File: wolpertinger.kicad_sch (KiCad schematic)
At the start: 19 parts, among them IC1 TL074

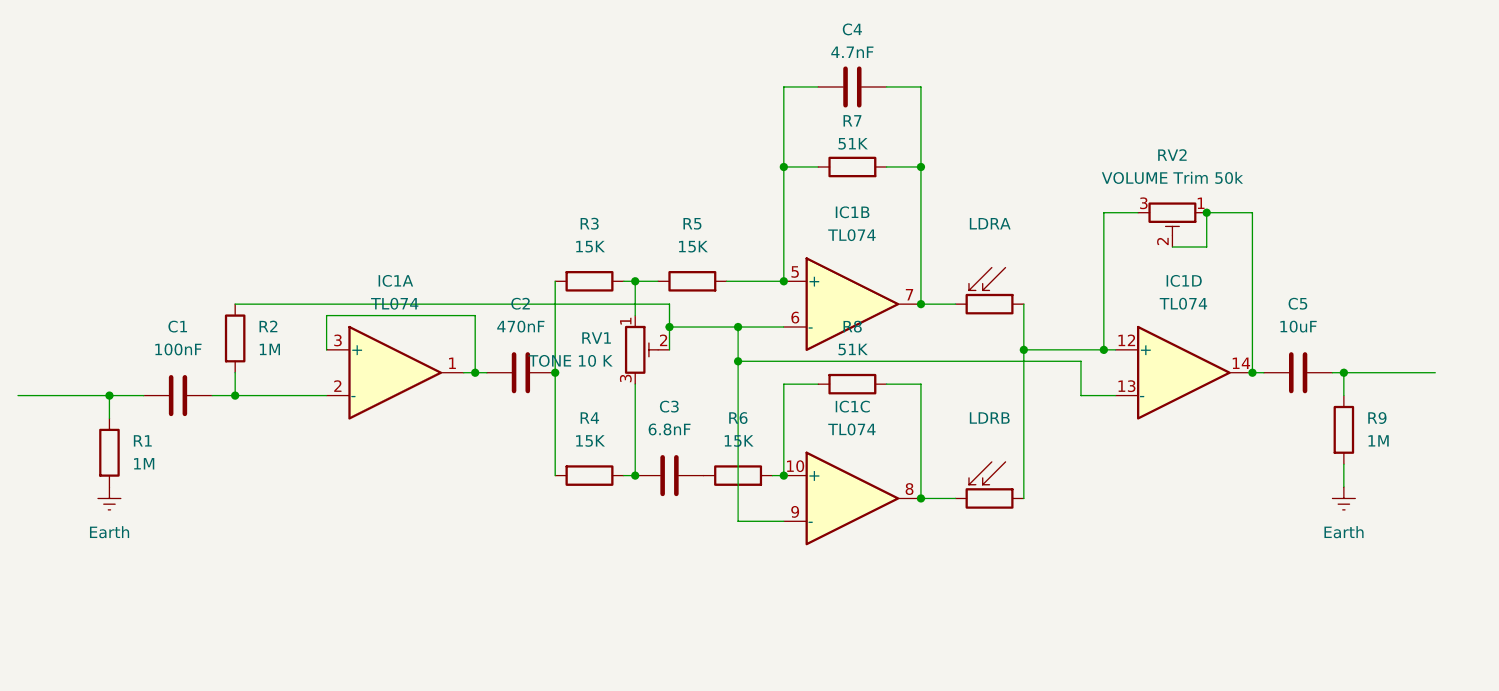
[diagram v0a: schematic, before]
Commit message: add gitignore and schematic cleanup
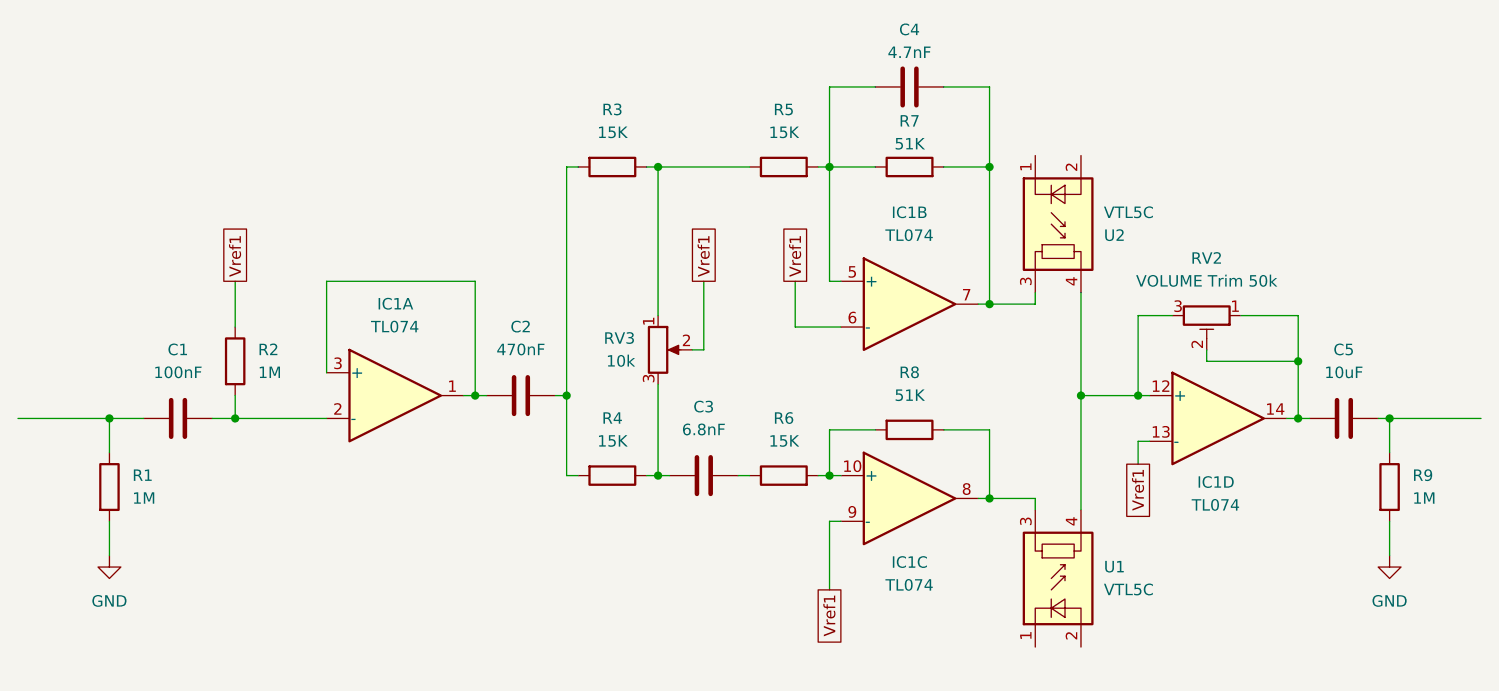
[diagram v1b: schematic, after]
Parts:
- removed LDRA, LDRB: (no value), OptoDevice:R_LDR_5.1x4.3mm_P3.4mm_Vertical, symbol Sensor_Optical:LDR07
- removed RV1: TONE 10 K, symbol Device:R_Potentiometer_Trim
- added RV3: 10k, symbol Device:R_Potentiometer
- added U1, U2: VTL5C, OptoDevice:PerkinElmer_VTL5C, symbol Isolator:VTL5C
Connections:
- net at R3.1, R5.1: now also RV3.1
- net Vref1: now reaches IC1.13 (-), IC1.6 (-), IC1.9 (-), R2.1
- net Vref1: now also RV3.2
- net at C3.1, R4.1: now also RV3.3
- net at IC1.12 (+), RV2.3: now also U1.4, U2.4
- net at IC1.8, R8.1: now also U1.3
- net at C4.2, IC1.7, R7.2: now also U2.3
- net Earth renamed GND
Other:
- moved on the sheet: C1, C2, C3, C4, C5, IC1A, IC1B, IC1C, IC1D, R1, R2, R3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

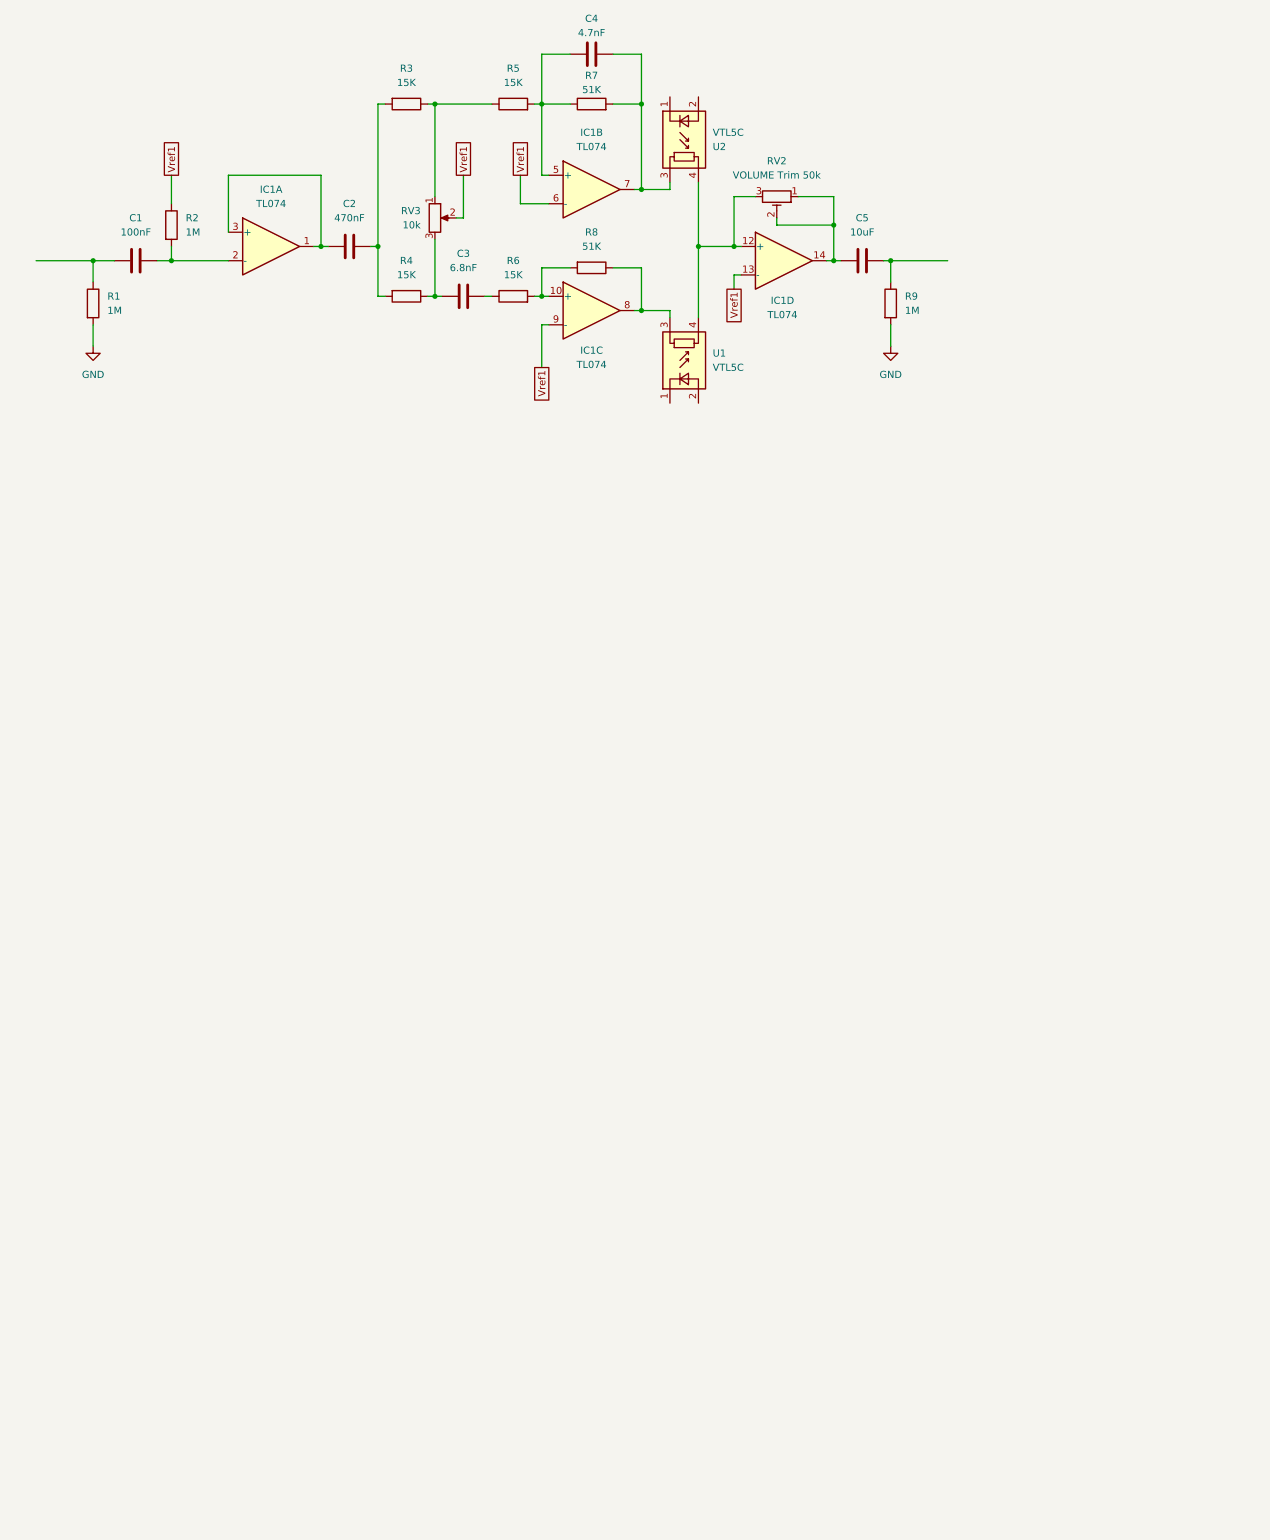
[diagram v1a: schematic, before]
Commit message: Add second channel and true bypass relay switching
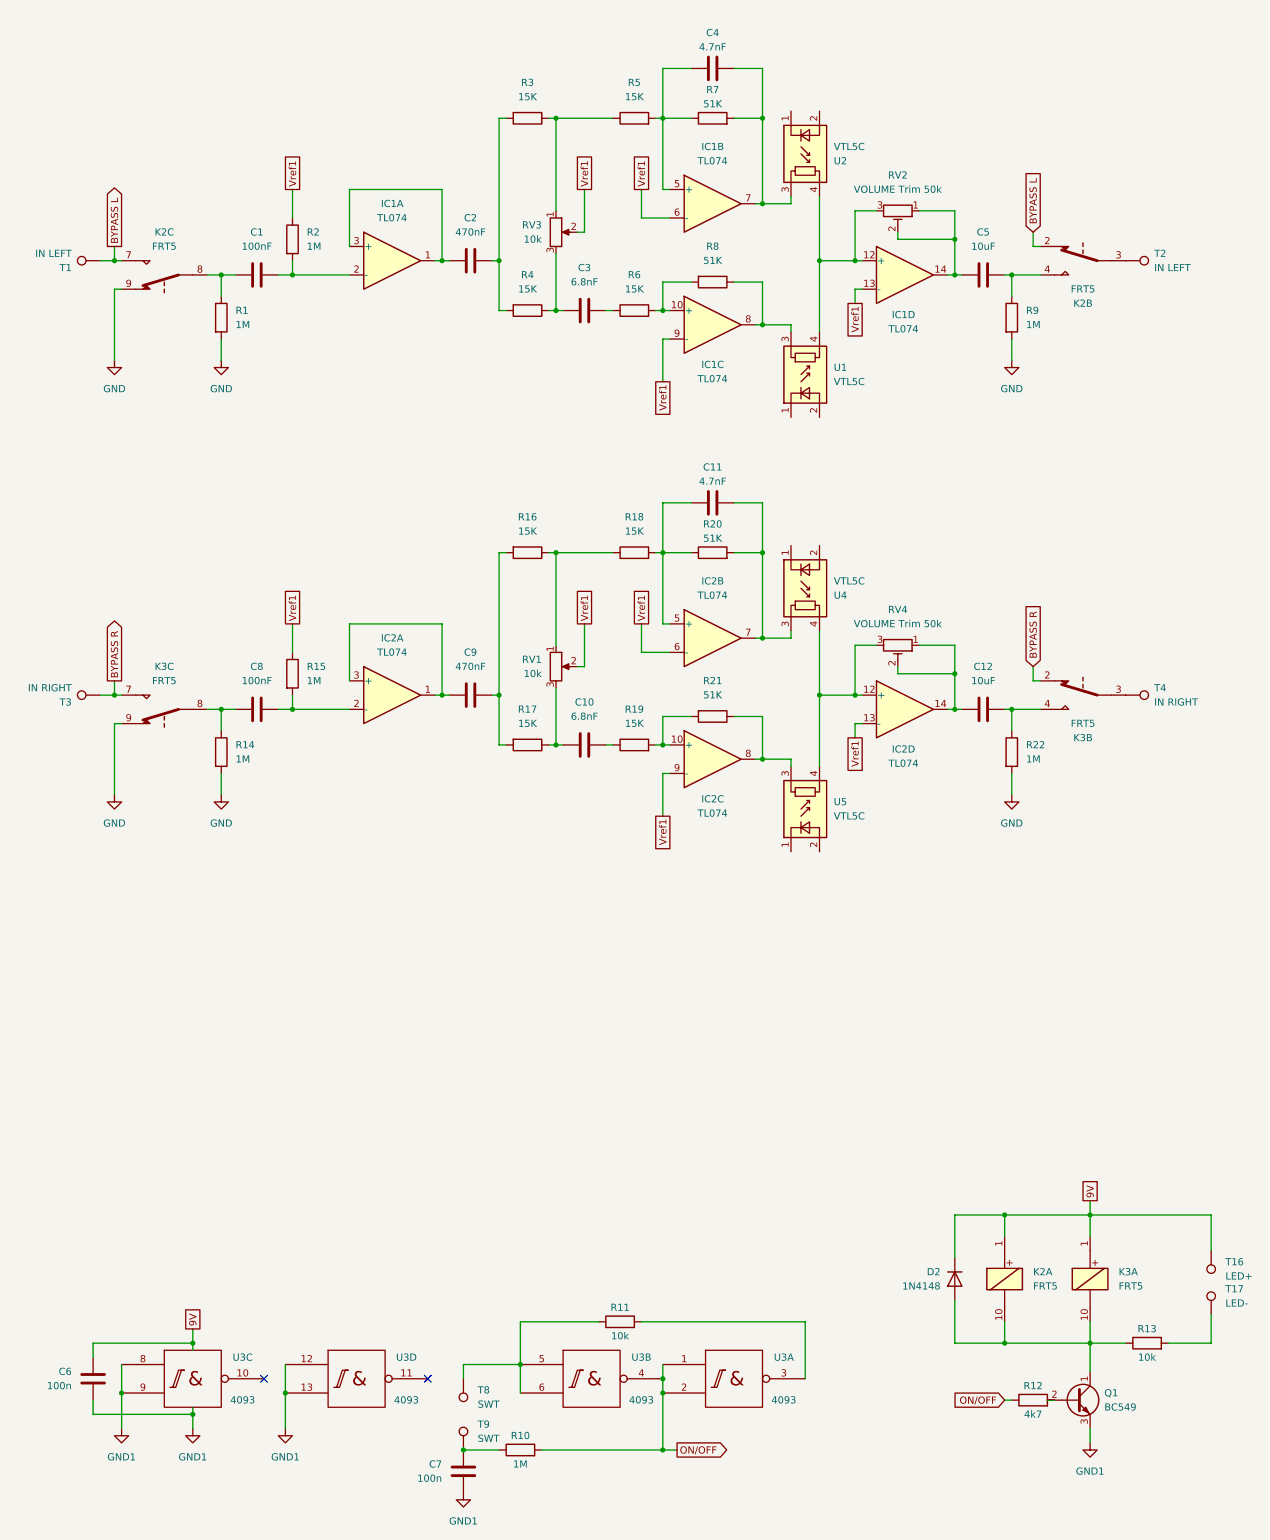
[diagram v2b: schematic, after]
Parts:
- added C10: 6.8nF, symbol Device:C
- added C11: 4.7nF, symbol Device:C
- added C12: 10uF, symbol Device:C
- added C6, C7: 100n, Capacitor_SMD:C_0805_2012Metric_Pad1.18x1.45mm_HandSolder, symbol Device:C
- added C8: 100nF, symbol Device:C
- added C9: 470nF, symbol Device:C
- added D2: 1N4148, Diode_THT:D_DO-35_SOD27_P7.62mm_Horizontal, symbol Diode:1N4148
- added IC2: TL074, symbol Amplifier_Operational:TL074
- added K2, K3: FRT5, Relay_THT:Relay_DPDT_FRT5, symbol Relay:FRT5_separated
- added Q1: BC549, Package_TO_SOT_THT:TO-92_Inline, symbol Transistor_BJT:BC549
- added R10: 1M, Resistor_SMD:R_0805_2012Metric_Pad1.20x1.40mm_HandSolder, symbol Device:R
- added R11, R13: 10k, Resistor_SMD:R_0805_2012Metric_Pad1.20x1.40mm_HandSolder, symbol Device:R
- added R12: 4k7, Resistor_SMD:R_0805_2012Metric_Pad1.20x1.40mm_HandSolder, symbol Device:R
- added R14, R15, R22: 1M, symbol Device:R
- added R16, R17, R18, R19: 15K, symbol Device:R
- added R20, R21: 51K, symbol Device:R
- added RV1: 10k, symbol Device:R_Potentiometer
- added RV4: VOLUME Trim 50k, symbol Device:R_Potentiometer_Trim
- added T1, T2: IN LEFT, Connector_Wire:SolderWire-0.5sqmm_1x01_D0.9mm_OD2.1mm, symbol Connector:TestPoint
- added T16: LED+, Connector_Wire:SolderWire-0.5sqmm_1x01_D0.9mm_OD2.1mm, symbol Connector:TestPoint
- added T17: LED-, Connector_Wire:SolderWire-0.5sqmm_1x01_D0.9mm_OD2.1mm, symbol Connector:TestPoint
- added T3, T4: IN RIGHT, Connector_Wire:SolderWire-0.5sqmm_1x01_D0.9mm_OD2.1mm, symbol Connector:TestPoint
- added T8, T9: SWT, Connector_Wire:SolderWire-0.5sqmm_1x01_D0.9mm_OD2.1mm, symbol Connector:TestPoint
- added U3: 4093, Package_SO:SO-14_3.9x8.65mm_P1.27mm, symbol 4xxx_IEEE:4093
- added U4, U5: VTL5C, OptoDevice:PerkinElmer_VTL5C, symbol Isolator:VTL5C
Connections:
- net GND: now also K2.9, K3.9, R14.2, R22.2
- net Vref1: now also IC2.13 (-), IC2.6 (-), IC2.9 (-), R15.1, RV1.2
- net at C1.1, R1.1: now also K2.8
- net at C5.2, R9.1: now also K2.4
- new net: D2.2 (A), K2.10, K3.10, Q1.1 (C), R13.1
- new net: K3.3, T4.1
- new net: C12.2, K3.4, R22.1
- new net: IC2.12 (+), RV4.3, U4.4, U5.4
- new net: C12.1, IC2.14, RV4.1, RV4.2
- new net: Q1.2 (B), R12.2
- new net: R11.1, T8.1, U3.5, U3.6
- new net: R11.2, U3.3
- new net: IC2.8, R21.1, U5.3
- new net: C11.2, IC2.7, R20.2, U4.3
- new net: C9.1, IC2.1, IC2.3 (+)
- new net: C8.2, IC2.2 (-), R15.2
- new net: R13.2, T17.1
- new net: C7.1, R10.1, T9.1
- new net: C8.1, K3.8, R14.1
- new net: K2.3, T2.1
- new net: IC2.10 (+), R19.2, R21.2
- new net: R16.1, R18.1, RV1.1
- new net: C11.1, IC2.5 (+), R18.2, R20.1
- new net: C10.1, R17.1, RV1.3
- new net: C10.2, R19.1
- new net: C9.2, R16.2, R17.2
- new net BYPASS L: K2.2, K2.7, T1.1
- new net BYPASS R: K3.2, K3.7, T3.1
- new net GND1: C6.2, C7.2, Q1.3 (E), U3.12, U3.13, U3.7 (Vss), U3.7 (Vss), U3.7 (Vss), U3.7 (Vss), U3.8, U3.9
- new net ON/OFF: R10.2, R12.1, U3.1, U3.2, U3.4
- new net Vdd: C6.1, D2.1 (K), K2.1, K3.1, T16.1, U3.14 (Vdd), U3.14 (Vdd), U3.14 (Vdd), U3.14 (Vdd)
- no-connect marks 0 -> 2
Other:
- moved on the sheet: C1, C2, C3, C4, C5, IC1A, IC1B, IC1C, IC1D, R1, R2, R3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

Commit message: section cleanup
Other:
- note added: "left channel"
- note added: "relay bypass"
- note added: "right channel"
- moved on the sheet: C10, C11, C12, C6, C7, C8, C9, D2, IC2A, IC2B, IC2C, IC2D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
